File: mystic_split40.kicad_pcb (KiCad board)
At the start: 2 copper layers, 220.5 x 98.8 mm, 149 parts, among them J1 RX, J15 RESET, J16 ISP, J17 WS2812, J18 SJ-43514-SMT, J2 TX, J22 AREF, J25 TYPE-C-31-M-12, J3 RX, J33 RESET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

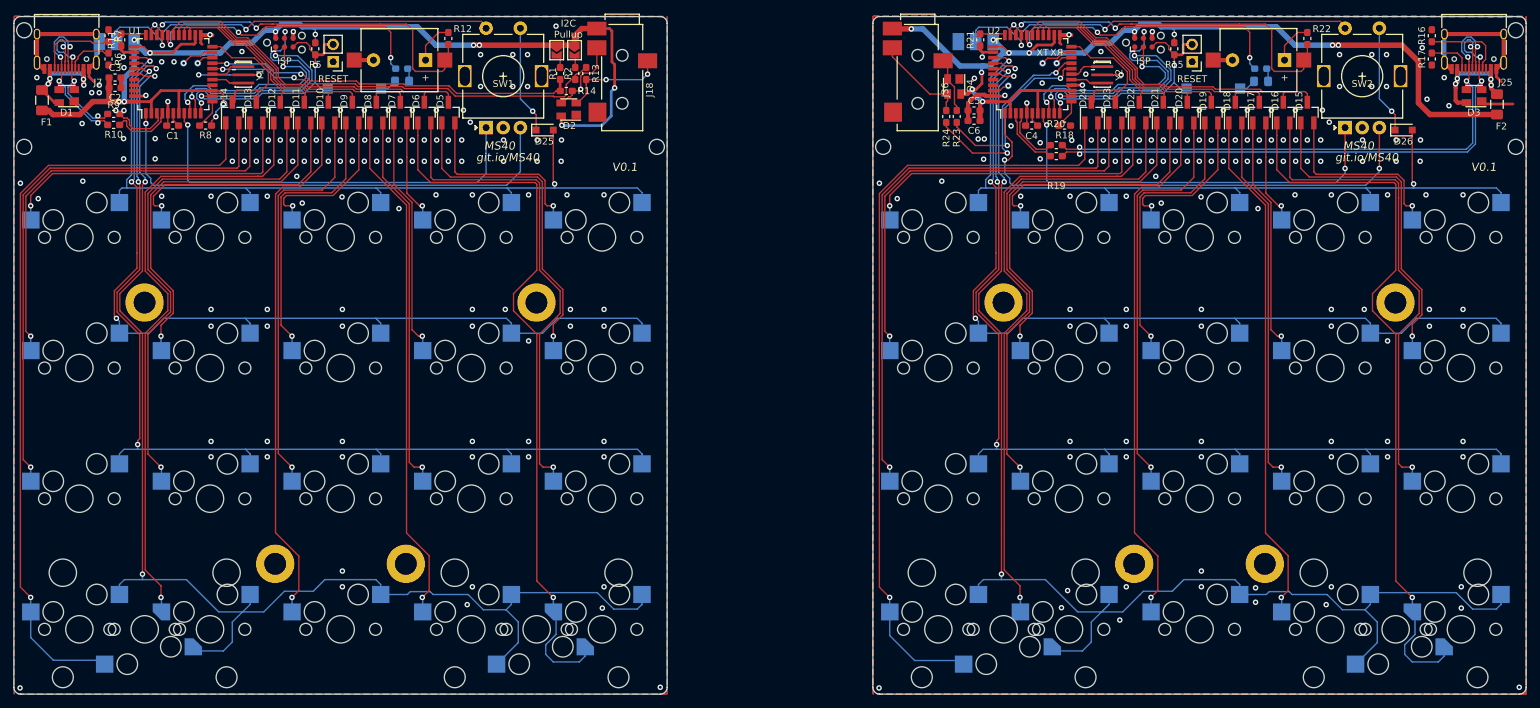
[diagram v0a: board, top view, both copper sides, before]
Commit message: Fixed up silkscreen
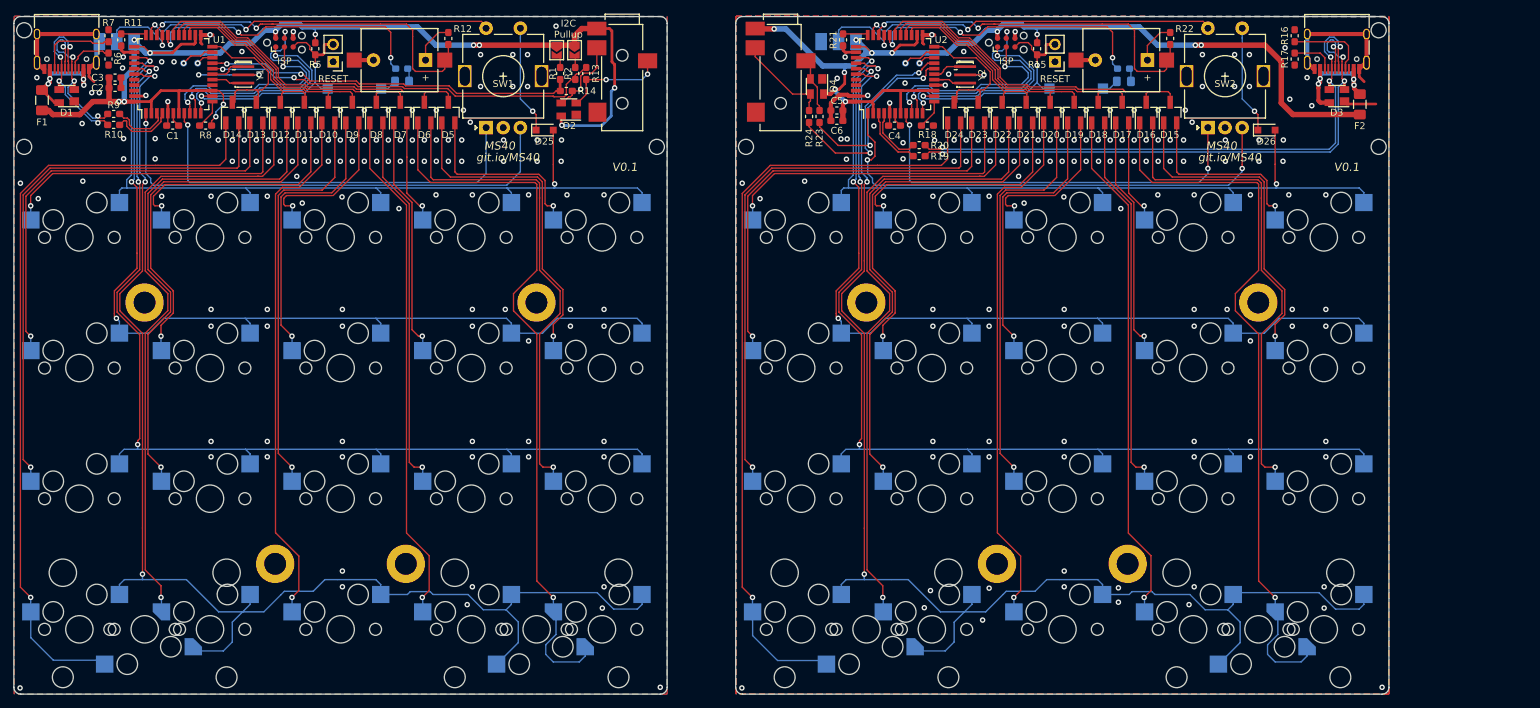
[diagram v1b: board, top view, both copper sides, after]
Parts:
- removed J22: AREF, TestPoint:TestPoint_Pad_D1.0mm
- moved BZ3 20.0 mm to (205.5, 19.1)
- moved BZ4 20.0 mm to (201.7, 19.1)
- moved C4 20.0 mm to (168.7, 28.6)
- moved C5 20.0 mm to (160.2, 26.4)
- moved C6 20.0 mm to (160.2, 27.9)
- moved D15 20.0 mm to (208.8, 26.7)
- moved D16 20.0 mm to (205.3, 26.7)
- moved D17 20.0 mm to (201.8, 26.7)
- moved D18 20.0 mm to (198.3, 26.7)
- moved D19 20.0 mm to (194.8, 26.7)
- moved D20 20.0 mm to (191.3, 26.7)
- moved D21 20.0 mm to (187.8, 26.7)
- moved D22 20.0 mm to (184.3, 26.7)
- moved D23 20.0 mm to (180.8, 26.7)
- moved D24 20.0 mm to (177.3, 26.7)
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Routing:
- net (no net): track 2.49 -> 0.00 mm, vias 2 -> 0
- net GND: vias 276 -> 273
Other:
- board size 220.5 x 98.8 mm -> 200.5 x 98.8 mm

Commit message: Moved WS2812 pads and added pinout
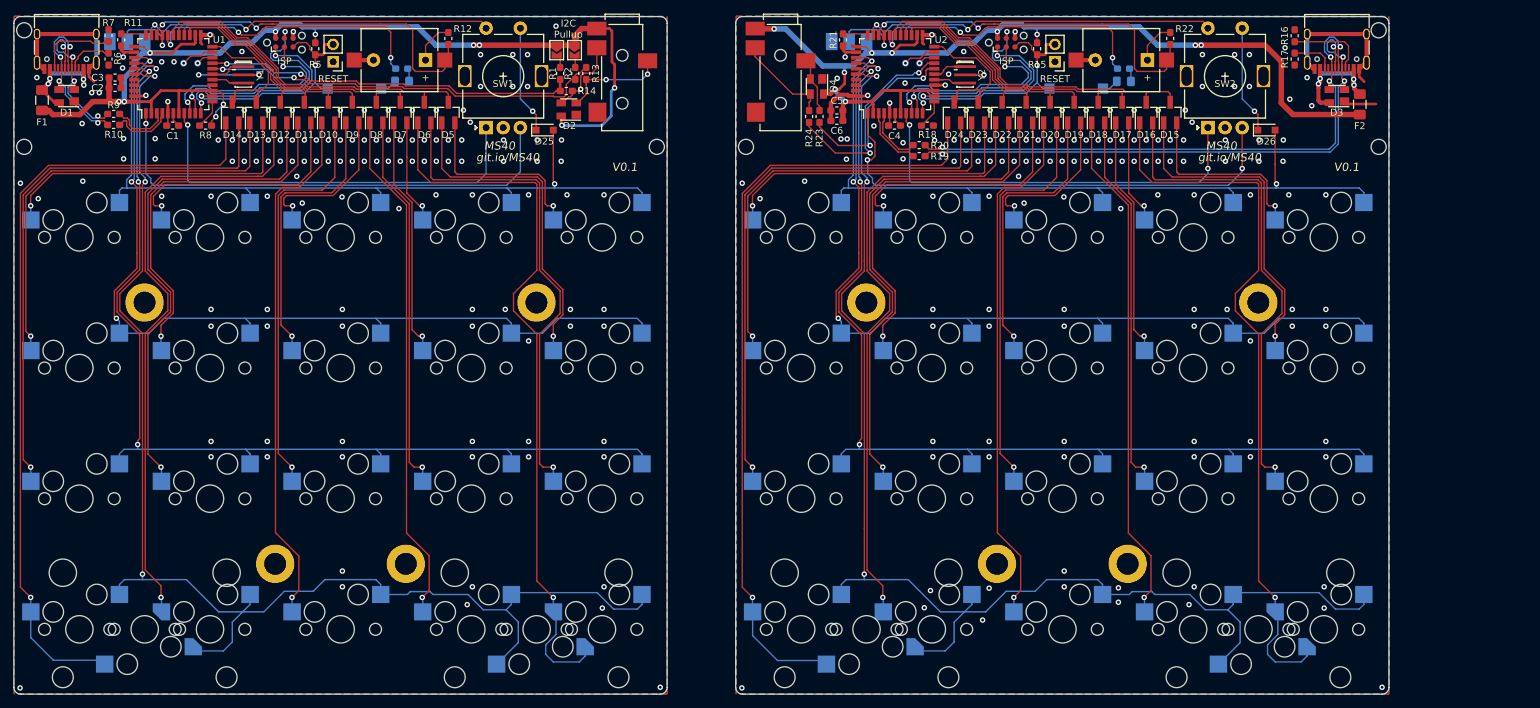
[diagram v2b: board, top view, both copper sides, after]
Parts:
- moved J17 1.54 mm to (54.2, 16.4)
- moved J35 1.54 mm to (159.5, 16.4)
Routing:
- net +5V: track 318.3 -> 315.5 mm, vias 23 -> 21
- net /Left MCU/WS2812_out: track 11.4 -> 9.83 mm
- net /Right MCU/WS2812_out: track 11.4 -> 9.83 mm
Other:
- board text added: "+ D -"
